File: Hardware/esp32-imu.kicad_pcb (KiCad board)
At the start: 2 copper layers, 95 x 35 mm, 14 parts, among them SW1 SW_MEC_5E, SW2 SW_MEC_5E

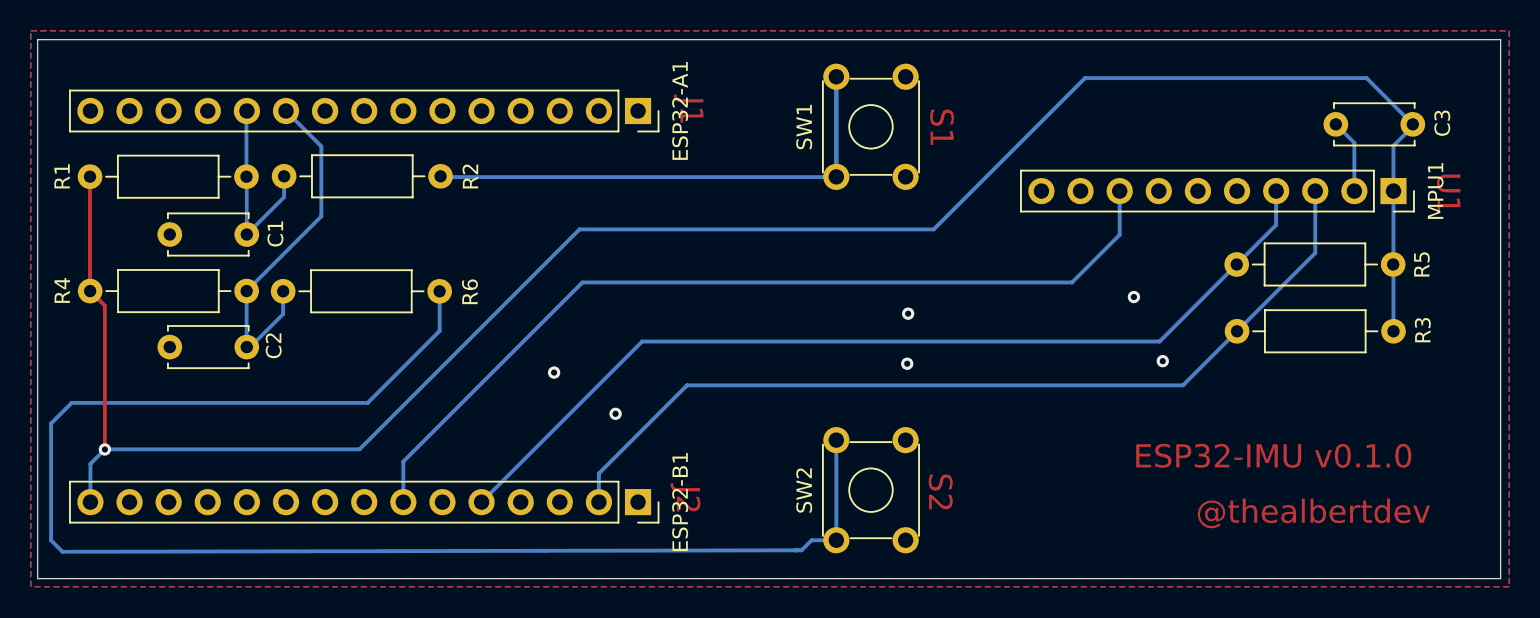
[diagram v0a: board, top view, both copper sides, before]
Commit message: Version with SMDs for externa external manufacturing
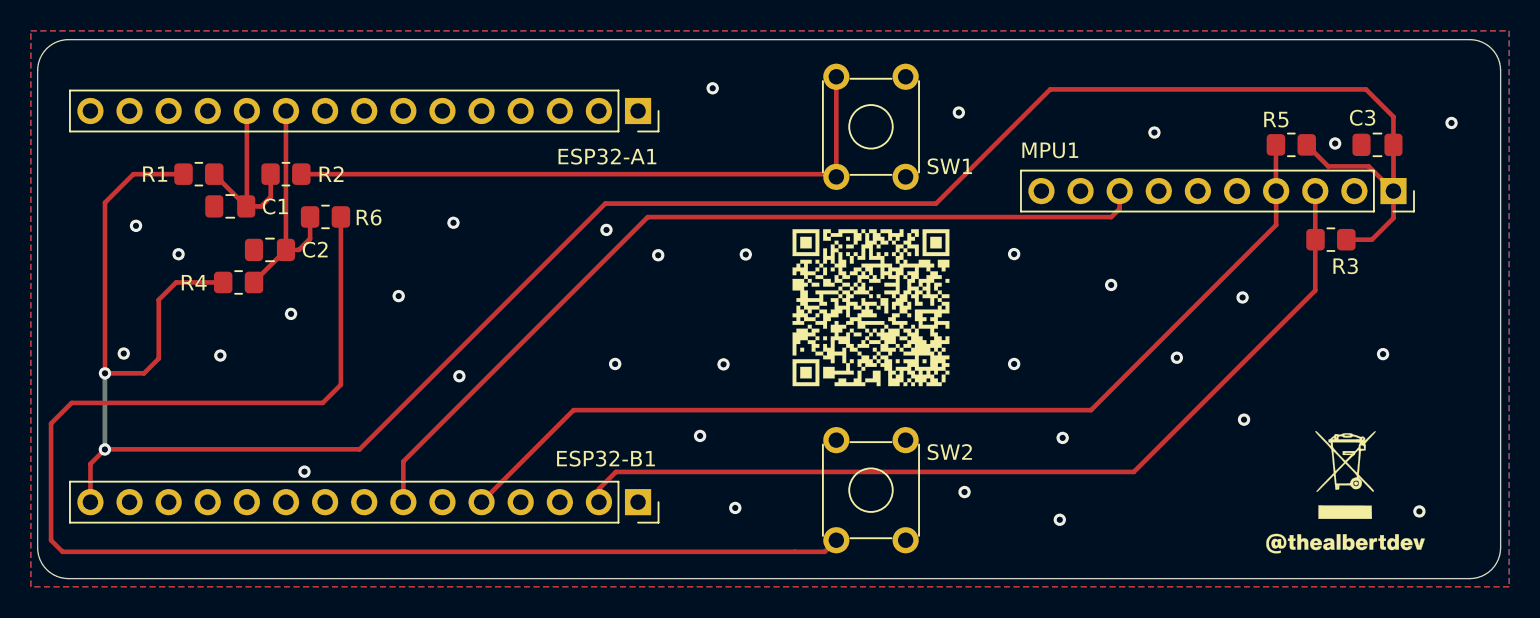
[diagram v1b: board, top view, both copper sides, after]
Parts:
- added G***: LOGO, AAC_Logos:Prototype-QR, F.Cu at (157.3, 99.7)
- added G***: LOGO, AAC_Logos:Trash, F.Cu at (188.2, 110.5)
- added G***: LOGO, AAC_Logos:TheAlbertDev, F.Cu at (188.1, 115.0)
- C1, C2, C3: footprint Capacitor_THT:C_Disc_D5.0mm_W2.5mm_P5.00mm -> Capacitor_SMD:C_0805_2012Metric_Pad1.18x1.45mm_HandSolder
- R1, R2, R3, R4, R5, R6: footprint Resistor_THT:R_Axial_DIN0207_L6.3mm_D2.5mm_P10.16mm_Horizontal -> Resistor_SMD:R_0805_2012Metric_Pad1.20x1.40mm_HandSolder
- moved R5 10.2 mm to (184.6, 89.1)
- moved R2 10.0 mm to (119.3, 91.0)
- moved R4 9.65 mm to (116.3, 98.1)
- moved R6 8.85 mm to (121.9, 93.8)
- moved R3 7.20 mm to (187.2, 95.3)
- moved R1 7.07 mm to (113.7, 91.0)
- moved C2 6.49 mm to (118.3, 95.9)
- moved C3 2.65 mm to (190.2, 89.1)
- moved C1 2.12 mm to (115.7, 93.1)
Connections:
- SW2 pad 2: Net-(R6-Pad1) -> (no net)
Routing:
- net +3V3: track 132.0 -> 149.3 mm, vias 1 -> 2
- net Net-(R2-Pad1): track 32.2 -> 41.3 mm
- net Net-(C2-Pad1): track 23.0 -> 15.4 mm
- net Net-(R6-Pad1): track 96.1 -> 90.0 mm
- net GND: track 4.83 -> 0.00 mm, vias 6 -> 32
- net /SDA: track 61.3 -> 64.3 mm
- net /INT: track 58.1 -> 57.1 mm
- net /SCL: track 58.3 -> 59.2 mm
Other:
- outline, holes or cut-outs redrawn
- board text removed: "@thealbertdev"
- board text removed: "ESP32-IMU v0.1.0"
- board text removed: "J1"
- board text removed: "J2"
- board text removed: "S1"
- board text removed: "S2"
- board text removed: "U1"
